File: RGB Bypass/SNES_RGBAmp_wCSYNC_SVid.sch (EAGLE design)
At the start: 25 parts, among them U1 THS7374

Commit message: go to version 4.1
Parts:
- removed U$2: THS7314, snes_div:THS7314
- added C, CS, Y: (no value), wirepad:SMD2
- added C43, C53: 330u, rcl:CPOL-EUSMCD
- added C44, C54, C64: 47p, rcl:C-EUC0603K
- added C63: 100n, rcl:C-EUC0603K
- added J2: (no value), jumper:SJ
- added R41: 9k53, rcl:R-EU_R0603
- added R42: 620, rcl:R-EU_R0603
- added R43, R53, R63: (no value), rcl:R-EU_R0603
- U$1: value SNES_MULTIAV_RGB_ONLY -> SNES_MULTIAV_RGBSYC; device snes_div:SNES_MULTIAV_RGB_ONLY -> snes_div:SNES_MULTIAV_RGBSYC
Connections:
- new net N$10: R41.1, R42.1, U1G$1.CI1
- new net N$11: R33.2, U1G$1.CO4
- new net N$12: C53.+, Y.P
- new net N$13: C.P, C63.2
- new net N$17: CS.P, R41.2
- new net N$18: C43.+, J2.1, U1G$1.CO1
- new net N$19: C43.-, J2.2, R43.2
- new net N$20: C53.-, R53.1
- new net N$21: C54.2, R53.2, U$1G$1.Y
- new net N$22: C64.2, R63.2, U$1G$1.C
- new net N$23: C63.1, R63.1
- net GND: now also C44.2, C54.1, C64.1, R42.2, U$1G$3.GND; no longer U$1G$1.GND, U$2G$2.GND, U1G$1.CI1
- net N$1: no longer U$2G$1.CI1
- net N$2: no longer U$2G$1.CI2
- net N$4: now also C44.1, R43.1, U$1G$1./CS; no longer R23.2, U$2G$1.CO2, U1G$1.CO3
- net N$5: now also U$1G$1.RED; no longer U$1G$3.RED
- net N$6: now also U$1G$1.GREEN; no longer U$1G$3.GREEN
- net N$7: now also R23.2, U1G$1.CO3; no longer R13.2, U$2G$1.CO1, U1G$1.CO2
- net N$8: now also R13.2, U1G$1.CO2; no longer R33.2, U$2G$1.CO3, U1G$1.CO4
- net N$9: now also U$1G$1.BLUE; no longer U$1G$3.BLUE
- net R9: no longer U$2G$1.CI3
- net VCC: now also U$1G$3.VCC; no longer U$1G$2.VCC, U$2G$2.VCC
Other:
- moved on the sheet: C14, C24, C34, R12, R22, R32

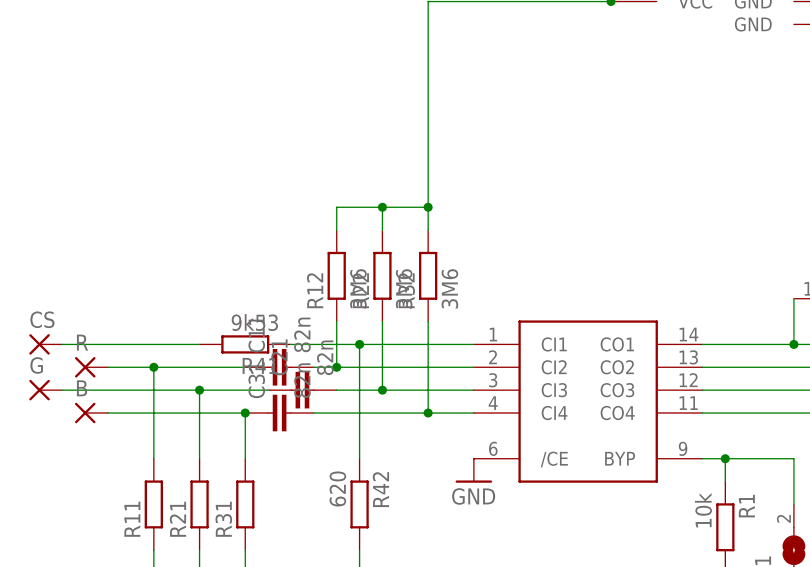
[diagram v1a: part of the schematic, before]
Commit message: Change resistor values
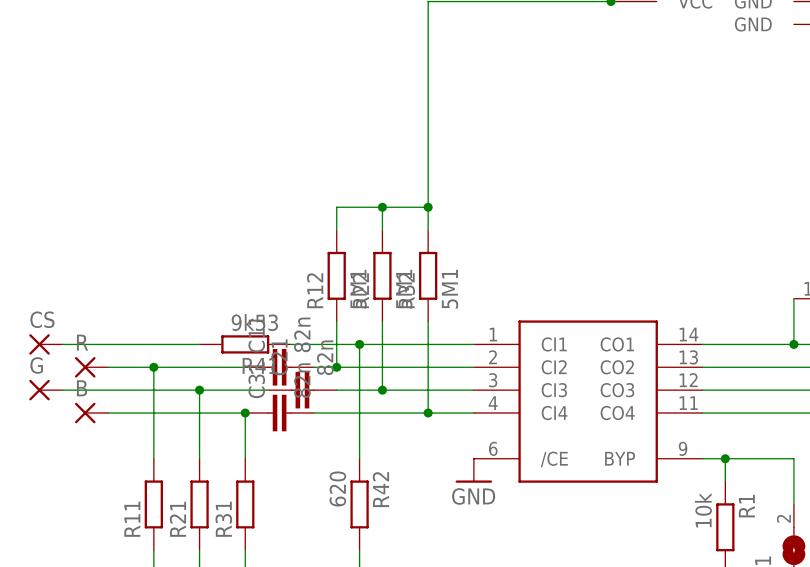
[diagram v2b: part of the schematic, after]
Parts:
- R12, R22, R32: value 3M6 -> 5M1
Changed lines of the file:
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@@
 <part name="R21" library="rcl" deviceset="R-EU_" device="R0603"/>
 <part name="R31" library="rcl" deviceset="R-EU_" device="R0603"/>
-<part name="R12" library="rcl" deviceset="R-EU_" device="R0603" value="3M6"/>
-<part name="R22" library="rcl" deviceset="R-EU_" device="R0603" value="3M6"/>
-<part name="R32" library="rcl" deviceset="R-EU_" device="R0603" value="3M6"/>
+<part name="R12" library="rcl" deviceset="R-EU_" device="R0603" value="5M1"/>
+<part name="R22" library="rcl" deviceset="R-EU_" device="R0603" value="5M1"/>
+<part name="R32" library="rcl" deviceset="R-EU_" device="R0603" value="5M1"/>
 <part name="R13" library="rcl" deviceset="R-EU_" device="R0603"/>
 <part name="R23" library="rcl" deviceset="R-EU_" device="R0603"/>
